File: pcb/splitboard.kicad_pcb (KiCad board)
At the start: 2 copper layers, 222.9 x 95.2 mm, 150 parts, among them IC1 ATMEGA32U4-MU, J1 Conn_02x05_Counter_Clockwise, J2 Conn_droite, J3 Conn_On_Off, Q1 Q_NPN_BCE, Q2 Q_NPN_BCE, SW1 SW_Push_LED, SW10 SW_Push_LED, SW101 SPST_TACT-KMR2, SW11 SW_Push_LED, SW12 SW_Push_LED, SW13 SW_Push_LED, SW14 SW_Push_LED, SW15 SW_Push_LED, SW16 SW_Push_LED, SW17 SW_Push_LED, SW18 SW_Push_LED, SW19 SW_Push_LED, SW2 SW_Push_LED, SW20 SW_Push_LED, SW21 SW_Push_LED, SW22 SW_Push_LED, SW23 SW_Push_LED, SW24 SW_Push_LED, SW25 SW_Push_LED, SW26 SW_Push_LED, SW27 SW_Push_LED, SW28 SW_Push_LED, SW29 SW_Push_LED, SW3 SW_Push_LED, SW30 SW_Push_LED, SW31 SW_Push_LED, SW32 SW_Push_LED, SW33 SW_Push_LED, SW34 SW_Push_LED, SW35 SW_Push_LED, SW36 SW_Push_LED, SW37 SW_Push_LED, SW38 SW_Push_LED, SW39 SW_Push_LED, SW40 SW_Push_LED, SW41 SW_Push_LED, SW42 SW_Push_LED, SW43 SW_Push_LED, SW44 SW_Push_LED, SW45 SW_Push_LED, SW46 SW_Push_LED, SW47 SW_Push_LED, SW5 SW_Push_LED, SW50 Rotary_Encoder, SW6 SW_Push_LED, SW7 SW_Push_LED, SW8 SW_Push_LED, SW9 SW_Push_LED, U1 TCA9555DBR, U2 TCA9555DBR, U3 MCP73831T-2ACI/OT, U4 SPX3819-3.3, U5 MBT40, X3 microUSB, Y1 8MHz

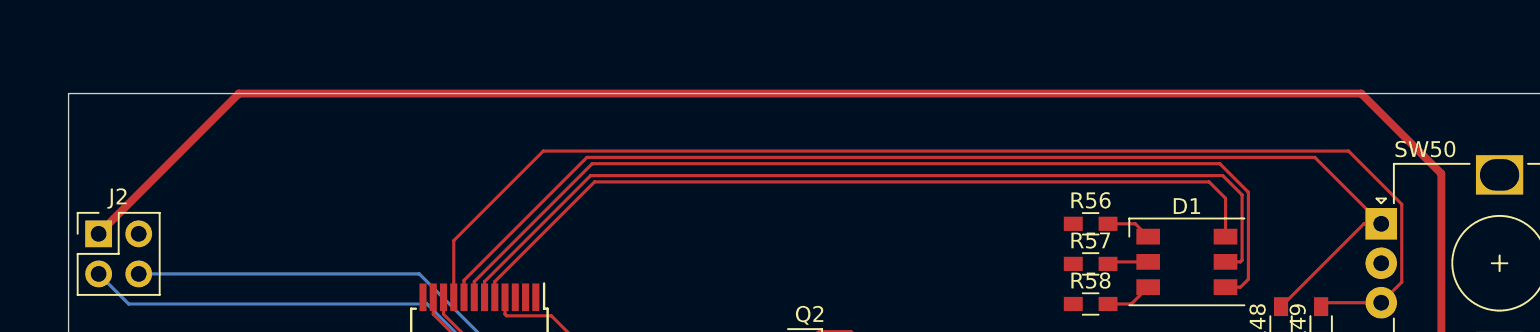
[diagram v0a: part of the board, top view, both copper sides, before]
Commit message: exported pcb to step/solidworks
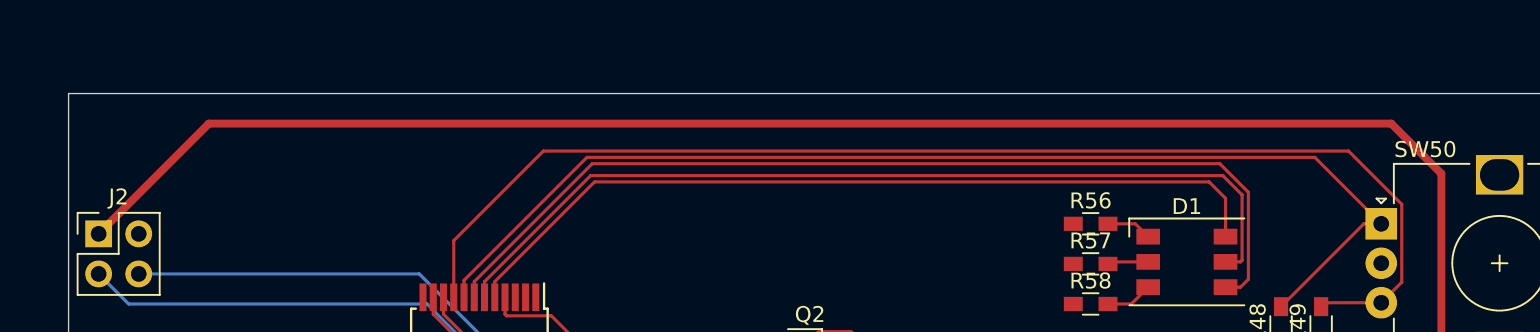
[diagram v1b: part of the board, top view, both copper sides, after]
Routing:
- net vcc1: track 175.1 -> 173.6 mm

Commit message: plan de masse gauche
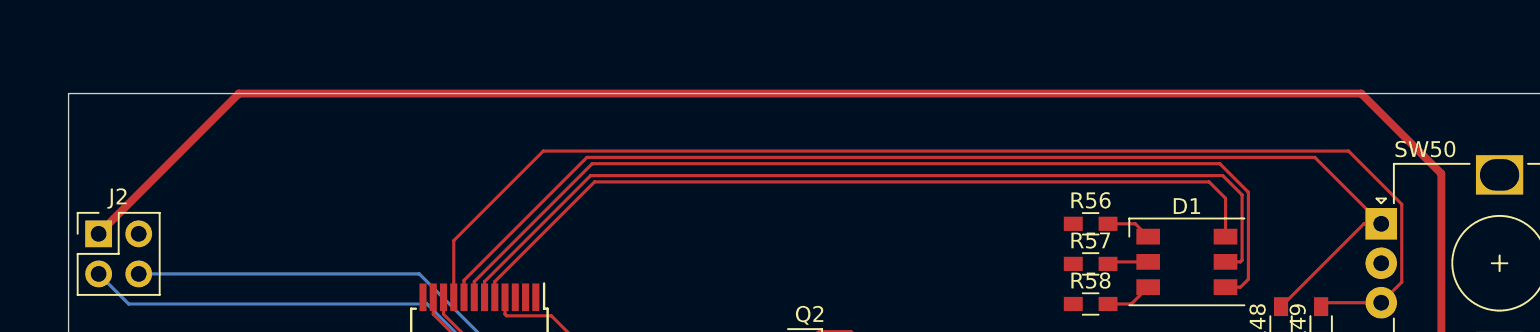
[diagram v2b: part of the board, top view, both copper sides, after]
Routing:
- net vcc1: track 173.6 -> 175.1 mm
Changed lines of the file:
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@@
   (general
     (thickness 1.6)
-    (drawings 47)
+    (drawings 46)
     (tracks 961)
     (zones 0)
@@
       (net 3 GND) (solder_mask_margin 0.0508))
   )
-  (dimension 45.72 (width 0.15) (layer Dwgs.User)
-    (gr_text "45,720 mm" (at 39.37 56.485) (layer Dwgs.User)
-      (effects (font (size 1 1) (thickness 0.15)))
-    )
-    (feature1 (pts (xy 62.23 59.69) (xy 62.23 57.198579)))
-    (feature2 (pts (xy 16.51 59.69) (xy 16.51 57.198579)))
-    (crossbar (pts (xy 16.51 57.785) (xy 62.23 57.785)))
-    (arrow1a (pts (xy 62.23 57.785) (xy 61.103496 58.371421)))
-    (arrow1b (pts (xy 62.23 57.785) (xy 61.103496 57.198579)))
-    (arrow2a (pts (xy 16.51 57.785) (xy 17.636504 58.371421)))
-    (arrow2b (pts (xy 16.51 57.785) (xy 17.636504 57.198579)))
-  )
   (gr_circle (center 52.07 86.36) (end 54.61 92.71) (layer Dwgs.User) (width 0.15))
   (gr_circle (center 90.17 142.875) (end 92.075 149.225) (layer Dwgs.User) (width 0.15))
@@
   (segment (start 160.695001 80.710001) (end 172.604999 80.710001) (width 0.2) (layer F.Cu) (net 5))
   (segment (start 159.785 79.8) (end 160.695001 80.710001) (width 0.2) (layer F.Cu) (net 5))
+  (segment (start 140.97 59.69) (end 132.08 68.58) (width 0.5) (layer F.Cu) (net 5))
+  (segment (start 215.9 77.47) (end 217.17 76.2) (width 0.5) (layer F.Cu) (net 5))
+  (segment (start 217.17 76.2) (end 217.17 64.77) (width 0.5) (layer F.Cu) (net 5))
+  (segment (start 212.09 59.69) (end 140.97 59.69) (width 0.5) (layer F.Cu) (net 5))
+  (segment (start 217.17 64.77) (end 212.09 59.69) (width 0.5) (layer F.Cu) (net 5))
   (segment (start 209.55 75.395) (end 209.55 77.47) (width 0.2) (layer F.Cu) (net 5))
+  (segment (start 209.55 77.47) (end 215.9 77.47) (width 0.5) (layer F.Cu) (net 5))
   (segment (start 208.28 77.47) (end 209.55 77.47) (width 0.5) (layer F.Cu) (net 5))
   (segment (start 207.01 75.395) (end 207.01 77.47) (width 0.2) (layer F.Cu) (net 5))
@@
   (segment (start 177.264999 76.050001) (end 177.264999 75.439999) (width 0.5) (layer F.Cu) (net 5))
   (segment (start 176.165 77.15) (end 177.264999 76.050001) (width 0.5) (layer F.Cu) (net 5))
-  (segment (start 213.995 61.595) (end 139.065 61.595) (width 0.5) (layer F.Cu) (net 5))
-  (segment (start 217.17 64.77) (end 213.995 61.595) (width 0.5) (layer F.Cu) (net 5))
-  (segment (start 217.17 76.2) (end 217.17 64.77) (width 0.5) (layer F.Cu) (net 5))
-  (segment (start 139.065 61.595) (end 132.08 68.58) (width 0.5) (layer F.Cu) (net 5))
-  (segment (start 215.9 77.47) (end 217.17 76.2) (width 0.5) (layer F.Cu) (net 5))
-  (segment (start 209.55 77.47) (end 215.9 77.47) (width 0.5) (layer F.Cu) (net 5))
   (segment (start 196.172 70.358) (end 196.045 70.485) (width 0.2) (layer F.Cu) (net 6))
   (segment (start 198.591 70.358) (end 196.172 70.358) (width 0.2) (layer F.Cu) (net 6))

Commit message: plan de masse gauche
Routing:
- net GND: track 47.7 -> 113.5 mm, vias 7 -> 130
- net +3V3: track 130.1 -> 155.3 mm, vias 1 -> 2
- net Net-(Q1-Pad3): track 476.6 -> 495.7 mm
- net /RST: track 13.8 -> 14.5 mm
- net Net-(SW5-Pad1): vias 1 -> 2
- added copper zone on B.Cu, net GND
- added copper zone on F.Cu, net GND

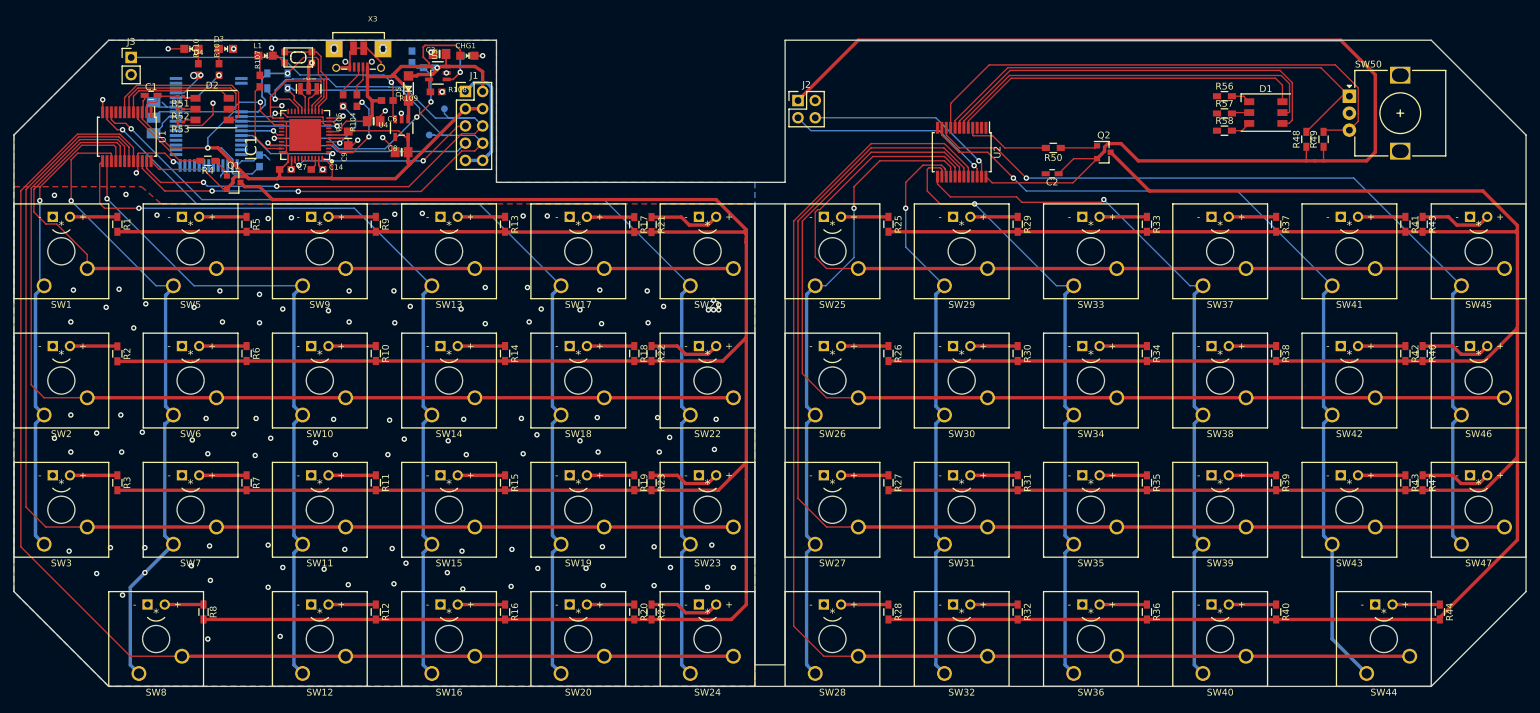
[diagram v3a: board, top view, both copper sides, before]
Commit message: plan de masse droite
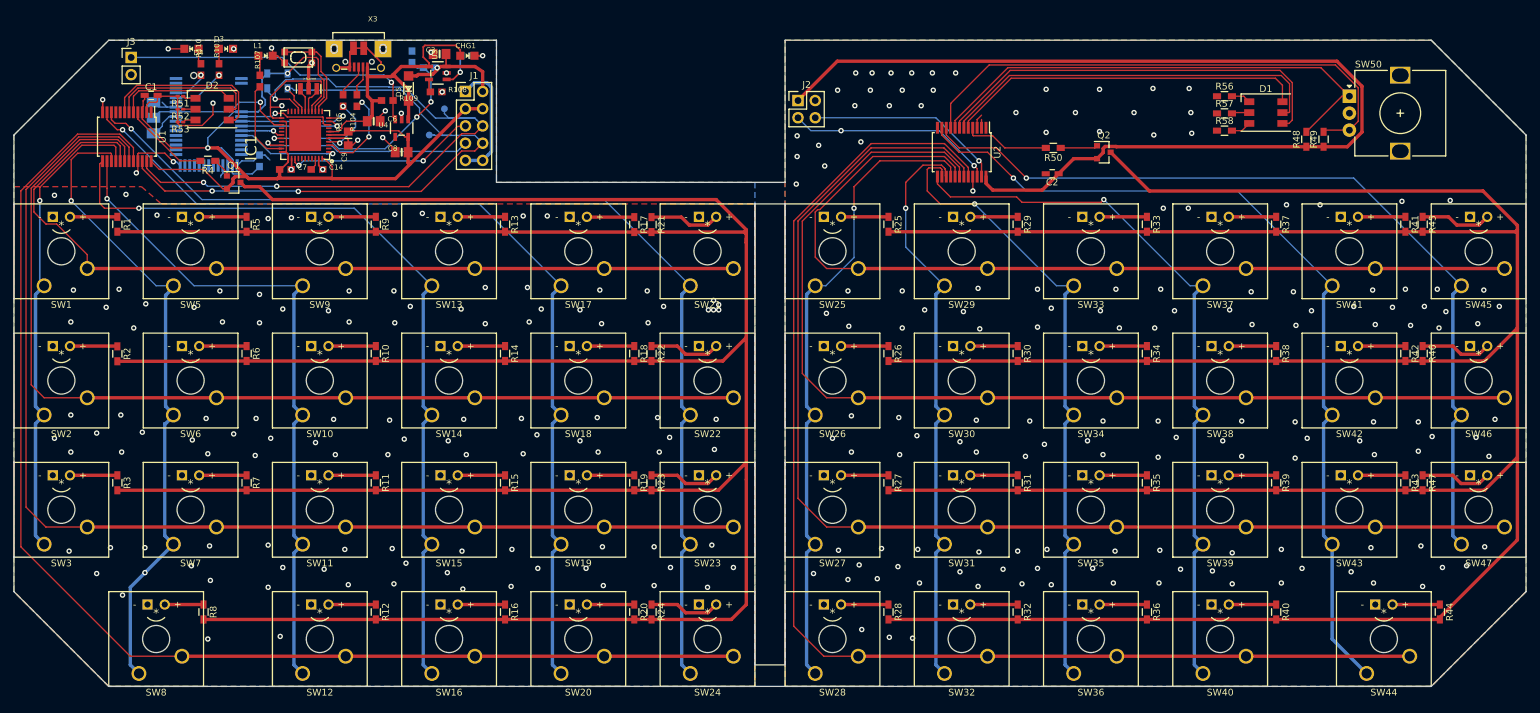
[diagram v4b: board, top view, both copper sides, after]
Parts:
- moved R110 0.38 mm to (44.1, 64.0)
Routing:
- net vcc1: track 175.1 -> 154.6 mm
- net gnd1: track 0.00 -> 5.48 mm, vias 0 -> 149
- net scl1: vias 1 -> 2
- added copper zone on B.Cu, net gnd1
- added copper zone on F.Cu, net gnd1

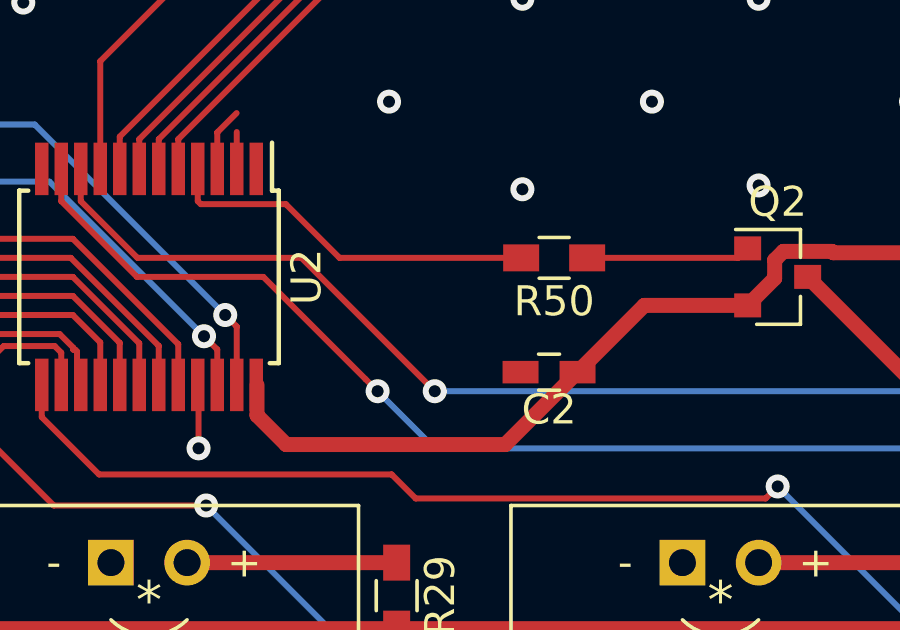
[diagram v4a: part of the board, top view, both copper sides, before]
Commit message: plan de masse droite
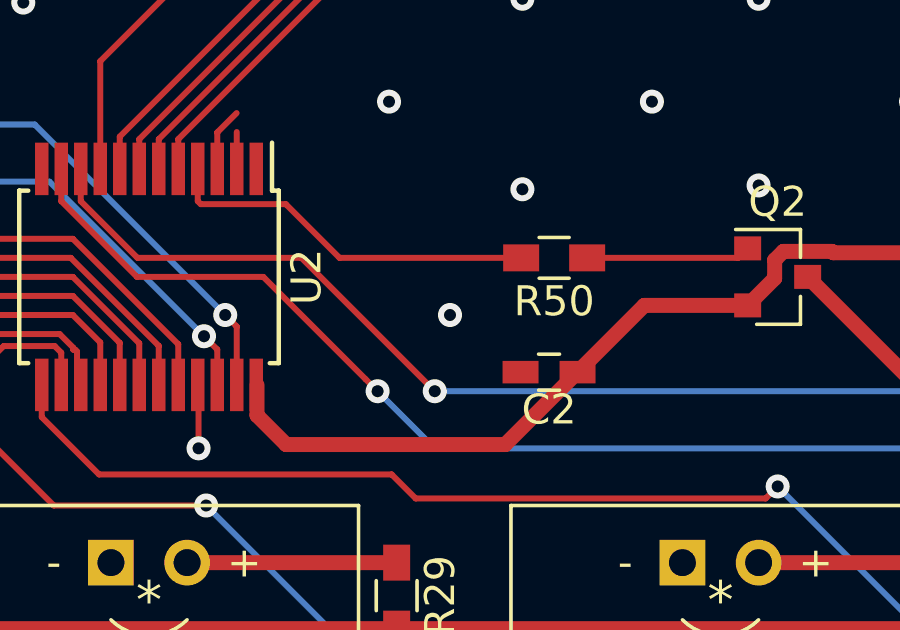
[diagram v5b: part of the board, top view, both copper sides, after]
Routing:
- net gnd1: vias 149 -> 150
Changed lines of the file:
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@@
     (thickness 1.6)
     (drawings 46)
-    (tracks 1313)
+    (tracks 1314)
     (zones 0)
     (modules 150)
@@
   (via (at 233.299 134.366) (size 0.8) (drill 0.4) (layers F.Cu B.Cu) (net 4))
   (via (at 230.632 137.16) (size 0.8) (drill 0.4) (layers F.Cu B.Cu) (net 4))
+  (via (at 166.243 77.47) (size 0.8) (drill 0.4) (layers F.Cu B.Cu) (net 4))
   (segment (start 213.056002 75.395) (end 209.55 75.395) (width 0.5) (layer F.Cu) (net 5))
   (segment (start 215.210011 66.477178) (end 215.210011 73.240991) (width 0.5) (layer F.Cu) (net 5))

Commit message: check wires
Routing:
- net vcc1: track 154.6 -> 157.0 mm
- net Net-(R49-Pad2): track 78.1 -> 79.0 mm
